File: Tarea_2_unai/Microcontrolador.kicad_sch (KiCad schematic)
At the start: 6 parts, among them IC2 ESP32-C3-MINI-1-N4X, J2 Conn_01x02_Pin

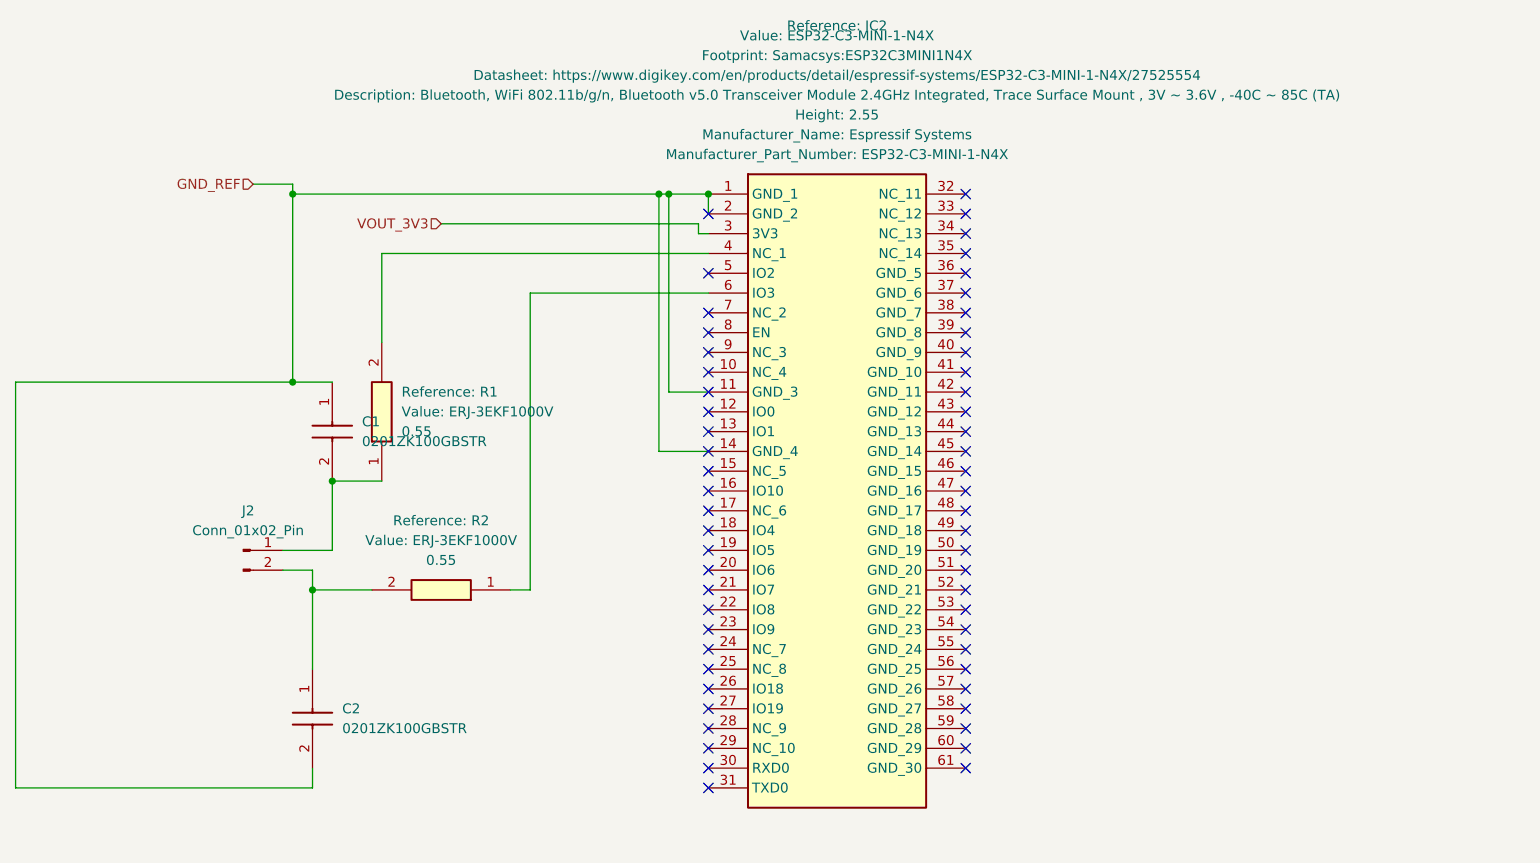
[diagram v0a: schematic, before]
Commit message: Sensores añadidos y nuevas capas añadidas
Falta por solucionar el enrutamiento de algunos pines de los sensores
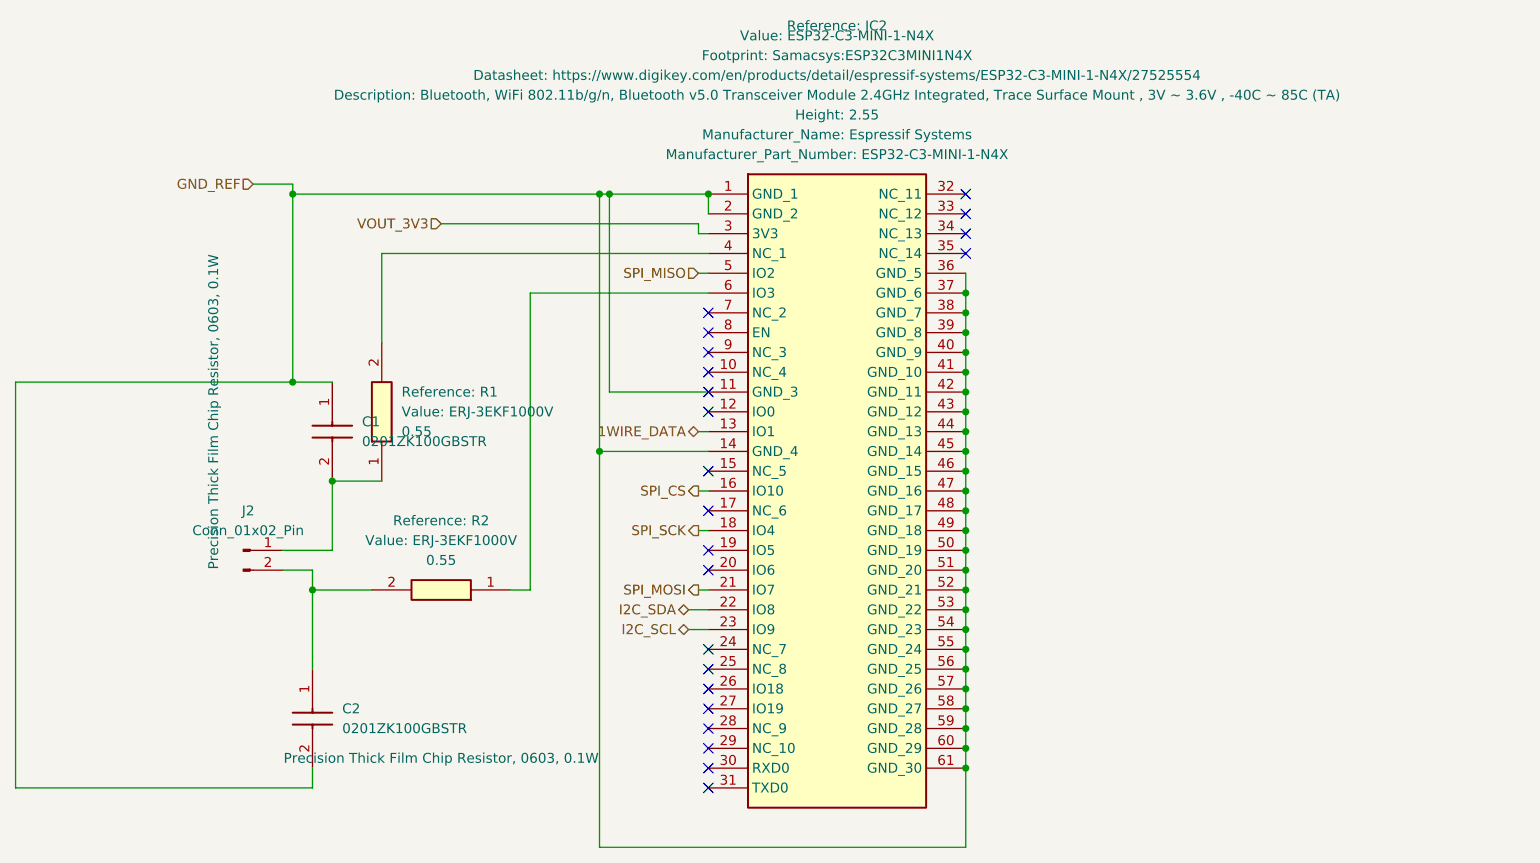
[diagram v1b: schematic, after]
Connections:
- net GND_REF: now also IC2.36 (GND_5), IC2.37 (GND_6), IC2.38 (GND_7), IC2.39 (GND_8), IC2.40 (GND_9), IC2.41 (GND_10), IC2.42 (GND_11), IC2.43 (GND_12), IC2.44 (GND_13), IC2.45 (GND_14), IC2.46 (GND_15), IC2.47 (GND_16), IC2.48 (GND_17), IC2.49 (GND_18), IC2.50 (GND_19), IC2.51 (GND_20), IC2.52 (GND_21), IC2.53 (GND_22), IC2.54 (GND_23), IC2.55 (GND_24), IC2.56 (GND_25), IC2.57 (GND_26), IC2.58 (GND_27), IC2.59 (GND_28), IC2.60 (GND_29), IC2.61 (GND_30)
- net 1WIRE_DATA: now reaches IC2.13 (IO1)
- net SPI_CS: now reaches IC2.16 (IO10)
- net SPI_SCK: now reaches IC2.18 (IO4)
- net SPI_MOSI: now reaches IC2.21 (IO7)
- net I2C_SDA: now reaches IC2.22 (IO8)
- net I2C_SCL: now reaches IC2.23 (IO9)
- net SPI_MISO: now reaches IC2.5 (IO2)
- no-connect marks 57 -> 22
